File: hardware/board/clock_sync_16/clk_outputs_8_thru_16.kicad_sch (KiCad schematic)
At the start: 40 parts, among them J2 AudioJack3, U5 ISO6521FREUR

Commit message: route pcb v0.1
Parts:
- removed C10 (x16): 1uF, Capacitor_SMD:C_0402_1005Metric, symbol Device:C
- removed D1 (x8): D_TVS, Diode_SMD:D_0402_1005Metric, symbol Device:D_TVS
- removed J2 (x8): AudioJack3, Connector_Audio:Jack_3.5mm_CUI_SJ-3523-SMT_Horizontal, symbol Connector:AudioJack3
- removed U5 (x8): ISO6521FREUR, kicad_component_library:DFN-8_3x2mm_P0.5mm, symbol kicad_component_library:ISO6521FREUR
- added C10 (x16): 1uF, Capacitor_SMD:C_0402_1005Metric, symbol Device:C
- added D1 (x8): D_TVS, Diode_SMD:D_0402_1005Metric, symbol Device:D_TVS
- added D11, D12, D22, D26, D27, D28, D29, D8: LED, LED_SMD:LED_0603_1608Metric_Pad1.05x0.95mm_HandSolder, symbol Device:LED
- added J2 (x8): AudioJack3, kicad_component_library:Jack_3.5mm_Kycon_STX-3680-5NB_Vertical, symbol Connector:AudioJack3
- added R13, R14, R15, R16, R4, R5, R6, R7: R, Resistor_SMD:R_0402_1005Metric, symbol Device:R
- added U5 (x8): ISO6521FREUR, kicad_component_library:DFN-8_3x2mm_P0.5mm, symbol kicad_component_library:ISO6521FREUR
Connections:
- net +3.3V: now also C10.1, C10.1, C10.1, C10.1, C10.1, C10.1, C10.1, C10.1, U5.1 (VCC1), U5.1 (VCC1), U5.1 (VCC1), U5.1 (VCC1), U5.1 (VCC1), U5.1 (VCC1), U5.1 (VCC1), U5.1 (VCC1)
- net CH10_CONNECTED: now also U5.2 (OUT)
- net CH11_CONNECTED: now also U5.2 (OUT)
- net CH12_CONNECTED: now also U5.2 (OUT)
- net CH13_CONNECTED: now also U5.2 (OUT)
- net CH14_CONNECTED: now also U5.2 (OUT)
- net CH15_CONNECTED: now also U5.2 (OUT)
- net CH8_CONNECTED: now also U5.2 (OUT)
- net CH9_CONNECTED: now also U5.2 (OUT)
- net GND: now also C10.2, C10.2, C10.2, C10.2, C10.2, C10.2, C10.2, C10.2, U5.4 (GND1), U5.4 (GND1), U5.4 (GND1), U5.4 (GND1), U5.4 (GND1), U5.4 (GND1), U5.4 (GND1), U5.4 (GND1)
- net HARP_CLKOUT: now also U5.3 (INB), U5.3 (INB), U5.3 (INB), U5.3 (INB), U5.3 (INB), U5.3 (INB), U5.3 (INB), U5.3 (INB)
- new net: C10.2, D1.1 (A1), D28.1 (K), J2.S, U5.5 (GND2)
- new net: D1.2 (A2), J2.T, U5.6 (OUTB) (x8)
- new net: C10.1, J2.R, R15.1, U5.7 (INA), U5.8 (VCC2)
- new net: C10.2, D1.1 (A1), D29.1 (K), J2.S, U5.5 (GND2)
- new net: C10.2, D1.1 (A1), D26.1 (K), J2.S, U5.5 (GND2)
- new net: C10.1, J2.R, R4.1, U5.7 (INA), U5.8 (VCC2)
- new net: C10.2, D1.1 (A1), D22.1 (K), J2.S, U5.5 (GND2)
- new net: C10.2, D1.1 (A1), D11.1 (K), J2.S, U5.5 (GND2)
- new net: C10.2, D1.1 (A1), D8.1 (K), J2.S, U5.5 (GND2)
- new net: C10.1, J2.R, R14.1, U5.7 (INA), U5.8 (VCC2)
- new net: C10.2, D1.1 (A1), D27.1 (K), J2.S, U5.5 (GND2)
- new net: D27.2 (A), R14.2
- new net: C10.1, J2.R, R13.1, U5.7 (INA), U5.8 (VCC2)
- new net: D28.2 (A), R15.2
- new net: C10.1, J2.R, R6.1, U5.7 (INA), U5.8 (VCC2)
- new net: D11.2 (A), R6.2
- new net: D8.2 (A), R5.2
- new net: C10.1, J2.R, R5.1, U5.7 (INA), U5.8 (VCC2)
- new net: D29.2 (A), R16.2
- new net: C10.1, J2.R, R16.1, U5.7 (INA), U5.8 (VCC2)
- new net: C10.2, D1.1 (A1), D12.1 (K), J2.S, U5.5 (GND2)
- new net: D12.2 (A), R7.2
- new net: C10.1, J2.R, R7.1, U5.7 (INA), U5.8 (VCC2)
- new net: D26.2 (A), R13.2
- new net: D22.2 (A), R4.2
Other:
- note removed: "Harp Clk Sync ESD Protection. Near J1."
- note removed: "Harp Clock Sync Emitter (UART0)"

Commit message: draft firmware
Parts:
- removed C10 (x16): 1uF, Capacitor_SMD:C_0402_1005Metric, symbol Device:C
- added C2 (x16): 100nF, Capacitor_SMD:C_0402_1005Metric, symbol Device:C
- R13, R14, R15, R16, R4, R5, R6, R7: value R -> 330; Link (none) -> https://www.digikey.com/en/products/detail/yageo/RC0402FR-0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
- U5: Manufacturer (none) -> Texas Instruments; Manufacturer Number (none) -> ISO6521FREUR
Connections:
- net +3.3V: now also C2.2, C2.2, C2.2, C2.2, C2.2, C2.2, C2.2, C2.2
- net GND: now also C2.1, C2.1, C2.1, C2.1, C2.1, C2.1, C2.1, C2.1
- net at D1.1 (A1), D28.1 (K), J2.S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: now also C2.2
- net at J2.R, R15.1, U5.7 (INA)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: now also C2.1
- net at D1.1 (A1), D29.1 (K), J2.S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: now also C2.2
- net at D1.1 (A1), D26.1 (K), J2.S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: now also C2.2
- net at J2.R, R4.1, U5.7 (INA)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: now also C2.1
- net at D1.1 (A1), D22.1 (K), J2.S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: now also C2.2
- net at D1.1 (A1), D11.1 (K), J2.S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: now also C2.2
- net at D1.1 (A1), D8.1 (K), J2.S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: now also C2.2
- net at J2.R, R14.1, U5.7 (INA)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: now also C2.1
- net at D1.1 (A1), D27.1 (K), J2.S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: now also C2.2
- net at J2.R, R13.1, U5.7 (INA)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: now also C2.1
- net at J2.R, R6.1, U5.7 (INA)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: now also C2.1
- net at J2.R, R5.1, U5.7 (INA)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: now also C2.1
- net at J2.R, R16.1, U5.7 (INA)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: now also C2.1
- net at D1.1 (A1), D12.1 (K), J2.S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: now also C2.2
- net at J2.R, R7.1, U5.7 (INA)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: now also C2.1

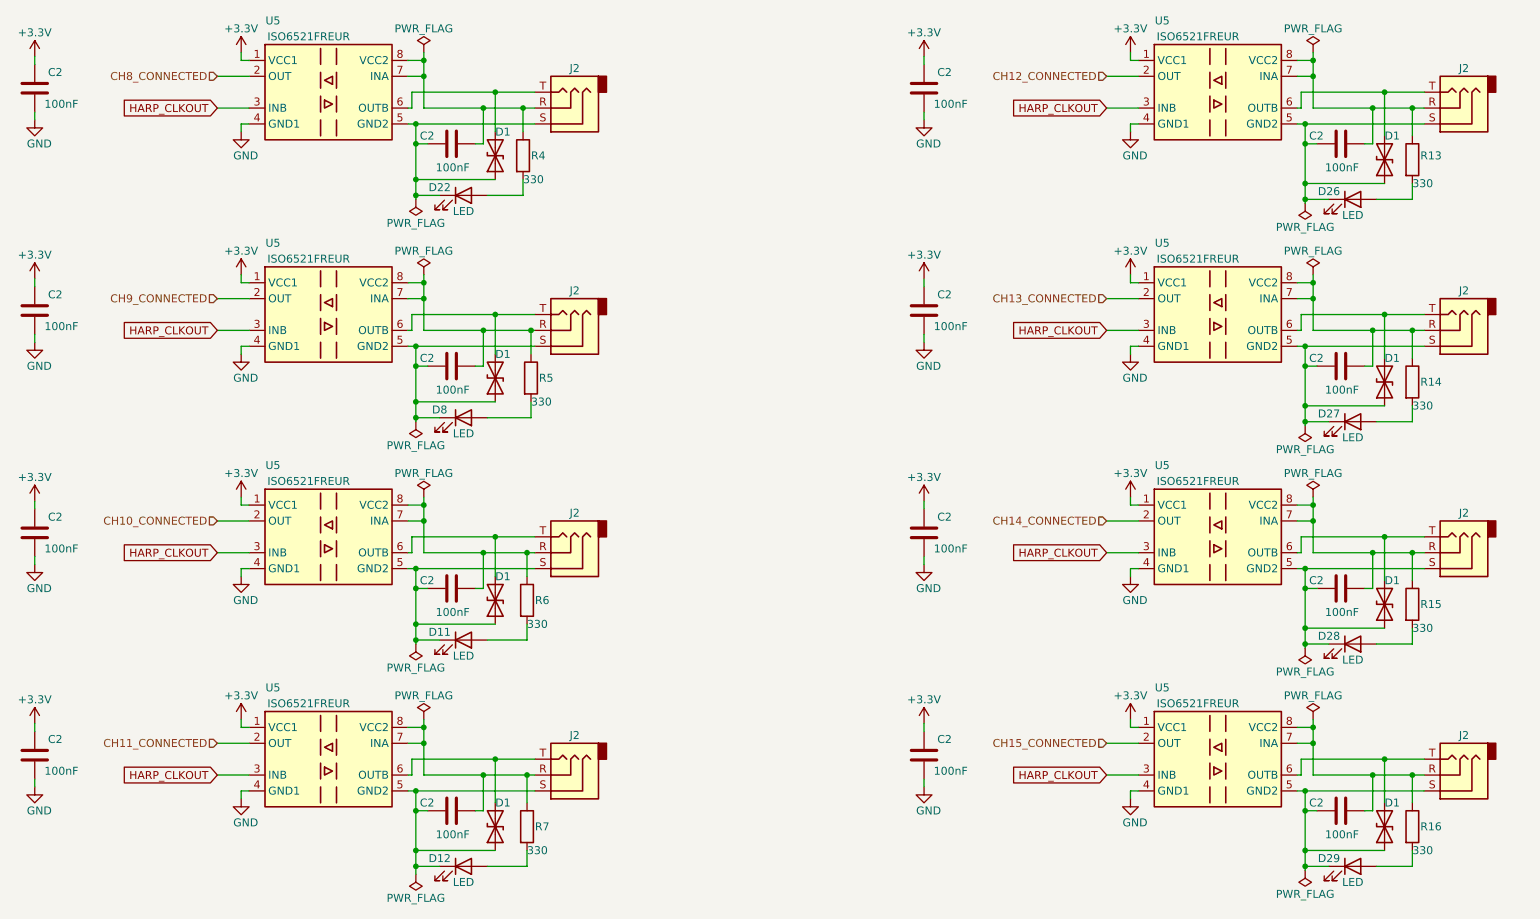
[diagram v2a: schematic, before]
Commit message: add pps/slow_uart output options
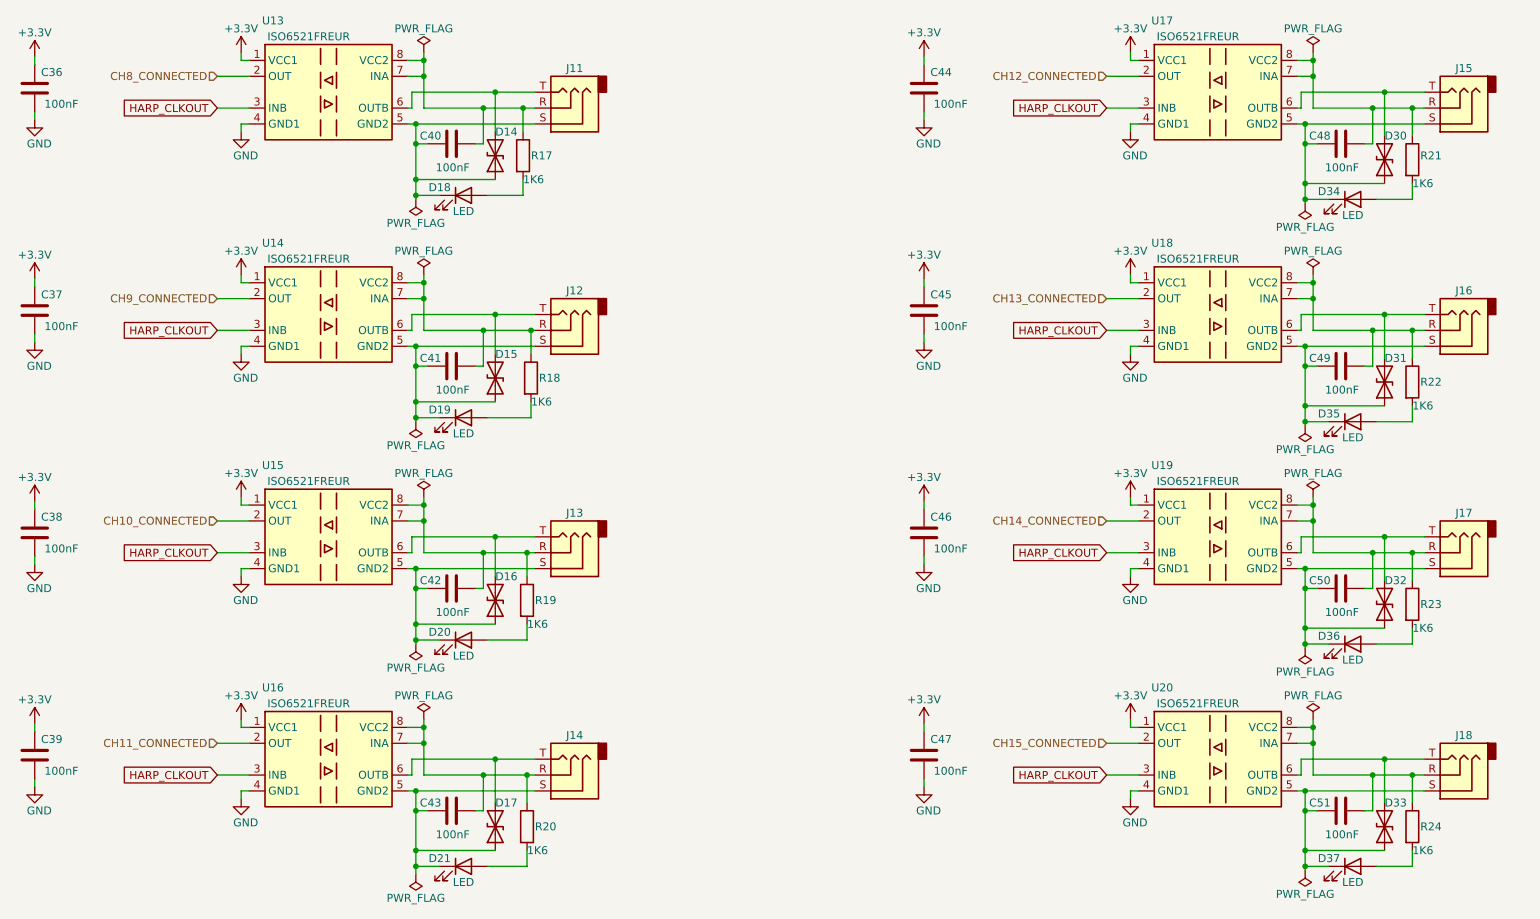
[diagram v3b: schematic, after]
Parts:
- R17: renamed from R4; value 330 -> 1K6; Link https://www.digikey.com/en/products/detail/yageo/RC0402FR-0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 -> https://www.digikey.com/en/products/detail/panasonic-electr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; Manufacturer Number RC0402FR-07330RL -> ERJ-2RKF1601X
- R18: renamed from R5; value 330 -> 1K6; Link https://www.digikey.com/en/products/detail/yageo/RC0402FR-0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 -> https://www.digikey.com/en/products/detail/panasonic-electr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; Manufacturer Number RC0402FR-07330RL -> ERJ-2RKF1601X
- R19: renamed from R6; value 330 -> 1K6; Link https://www.digikey.com/en/products/detail/yageo/RC0402FR-0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 -> https://www.digikey.com/en/products/detail/panasonic-electr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; Manufacturer Number RC0402FR-07330RL -> ERJ-2RKF1601X
- R20: renamed from R7; value 330 -> 1K6; Link https://www.digikey.com/en/products/detail/yageo/RC0402FR-0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 -> https://www.digikey.com/en/products/detail/panasonic-electr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; Manufacturer Number RC0402FR-07330RL -> ERJ-2RKF1601X
- R21: renamed from R13; value 330 -> 1K6; Link https://www.digikey.com/en/products/detail/yageo/RC0402FR-0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 -> https://www.digikey.com/en/products/detail/panasonic-electr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; Manufacturer Number RC0402FR-07330RL -> ERJ-2RKF1601X
- R22: renamed from R14; value 330 -> 1K6; Link https://www.digikey.com/en/products/detail/yageo/RC0402FR-0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 -> https://www.digikey.com/en/products/detail/panasonic-electr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; Manufacturer Number RC0402FR-07330RL -> ERJ-2RKF1601X
- R23: renamed from R15; value 330 -> 1K6; Link https://www.digikey.com/en/products/detail/yageo/RC0402FR-0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 -> https://www.digikey.com/en/products/detail/panasonic-electr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; Manufacturer Number RC0402FR-07330RL -> ERJ-2RKF1601X
- R24: renamed from R16; value 330 -> 1K6; Link https://www.digikey.com/en/products/detail/yageo/RC0402FR-0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 -> https://www.digikey.com/en/products/detail/panasonic-electr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; Manufacturer Number RC0402FR-07330RL -> ERJ-2RKF1601X
- renumbered C2 to C36, C2 to C37, C2 to C38, C2 to C39, C2 to C40, C2 to C41, C2 to C42, C2 to C43, C2 to C44, C2 to C45, C2 to C46, C2 to C47, C2 to C48, C2 to C49, C2 to C50, C2 to C51, D1 to D14, D1 to D15, D1 to D16, D1 to D17, D22 to D18, D8 to D19, D11 to D20, D12 to D21, D1 to D30, D1 to D31, D1 to D32, D1 to D33, D26 to D34, D27 to D35, D28 to D36, D29 to D37, J2 to J11, J2 to J12, J2 to J13, J2 to J14, J2 to J15, J2 to J16, J2 to J17, J2 to J18, U5 to U13, U5 to U14, U5 to U15, U5 to U16, U5 to U17, U5 to U18, U5 to U19, U5 to U20

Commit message: update harp core; update led resistors and deprecated parts; bump versions
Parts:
- D14, D15, D16, D17, D30, D31, D32, D33: Link https://www.digikey.com/en/products/detail/onsemi/ESD7571N2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 -> https://www.digikey.com/en/products/detail/nexperia-usa-inc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; Manufacturer Number ESD7571N2T5G -> PESD5V0F1BLD,315
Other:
- company: (none) -> The Allen Institute
- title: (none) -> harp.device.white-rabbit
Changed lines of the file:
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@@
 	(generator_version "8.0")
 	(paper "A4")
+	(title_block
+		(title "harp.device.white-rabbit")
+		(date "2025-02-21")
+		(rev "1.0.0")
+		(company "The Allen Institute")
+	)
 	(junction
 		(at 91.44 26.035)
@@
 			)
 		)
-		(property "Datasheet" "https://www.onsemi.com/pdf/datasheet/esd7571-d.pdf"
+		(property "Datasheet" "https://assets.nexperia.com/documents/data-sheet/PESD5V0F1BLD.pdf"
 			(at 245.11 146.05 0)
 			(effects
@@
 			)
 		)
-		(property "Link" "https://www.digikey.com/en/products/detail/onsemi/ESD7571N2T5G/7220690"
+		(property "Link" "https://www.digikey.com/en/products/detail/nexperia-usa-inc/PESD5V0F1BLD-315/3679473"
 			(at 245.11 146.05 0)
 			(effects
@@
 			)
 		)
-		(property "Manufacturer Number" "ESD7571N2T5G"
+		(property "Manufacturer Number" "PESD5V0F1BLD,315"
 			(at 245.11 146.05 0)
 			(effects
@@
 			)
 		)
-		(property "Datasheet" "https://www.onsemi.com/pdf/datasheet/esd7571-d.pdf"
+		(property "Datasheet" "https://assets.nexperia.com/documents/data-sheet/PESD5V0F1BLD.pdf"
 			(at 245.11 39.37 0)
 			(effects
@@
 			)
 		)
-		(property "Link" "https://www.digikey.com/en/products/detail/onsemi/ESD7571N2T5G/7220690"
+		(property "Link" "https://www.digikey.com/en/products/detail/nexperia-usa-inc/PESD5V0F1BLD-315/3679473"
 			(at 245.11 39.37 0)
 			(effects
@@
 			)
 		)
-		(property "Manufacturer Number" "ESD7571N2T5G"
+		(property "Manufacturer Number" "PESD5V0F1BLD,315"
 			(at 245.11 39.37 0)
 			(effects
@@
 			)
 		)
-		(property "Datasheet" "https://www.onsemi.com/pdf/datasheet/esd7571-d.pdf"
+		(property "Datasheet" "https://assets.nexperia.com/documents/data-sheet/PESD5V0F1BLD.pdf"
 			(at 102.87 109.855 0)
 			(effects
@@
 			)
 		)
-		(property "Link" "https://www.digikey.com/en/products/detail/onsemi/ESD7571N2T5G/7220690"
+		(property "Link" "https://www.digikey.com/en/products/detail/nexperia-usa-inc/PESD5V0F1BLD-315/3679473"
 			(at 102.87 109.855 0)
 			(effects
@@
 			)
 		)
-		(property "Manufacturer Number" "ESD7571N2T5G"
+		(property "Manufacturer Number" "PESD5V0F1BLD,315"
 			(at 102.87 109.855 0)
 			(effects
@@
 			)
 		)
-		(property "Datasheet" "https://www.onsemi.com/pdf/datasheet/esd7571-d.pdf"
+		(property "Datasheet" "https://assets.nexperia.com/documents/data-sheet/PESD5V0F1BLD.pdf"
 			(at 102.87 74.295 0)
 			(effects
@@
 			)
 		)
-		(property "Link" "https://www.digikey.com/en/products/detail/onsemi/ESD7571N2T5G/7220690"
+		(property "Link" "https://www.digikey.com/en/products/detail/nexperia-usa-inc/PESD5V0F1BLD-315/3679473"
 			(at 102.87 74.295 0)
 			(effects
@@
 			)
 		)
-		(property "Manufacturer Number" "ESD7571N2T5G"
+		(property "Manufacturer Number" "PESD5V0F1BLD,315"
 			(at 102.87 74.295 0)
 			(effects
@@
 			)
 		)
-		(property "Datasheet" "https://www.onsemi.com/pdf/datasheet/esd7571-d.pdf"
+		(property "Datasheet" "https://assets.nexperia.com/documents/data-sheet/PESD5V0F1BLD.pdf"
 			(at 245.11 74.93 0)
 			(effects
@@
 			)
 		)
-		(property "Link" "https://www.digikey.com/en/products/detail/onsemi/ESD7571N2T5G/7220690"
+		(property "Link" "https://www.digikey.com/en/products/detail/nexperia-usa-inc/PESD5V0F1BLD-315/3679473"
 			(at 245.11 74.93 0)
 			(effects
@@
 			)
 		)
-		(property "Manufacturer Number" "ESD7571N2T5G"
+		(property "Manufacturer Number" "PESD5V0F1BLD,315"
 			(at 245.11 74.93 0)
 			(effects
@@
 			)
 		)
-		(property "Datasheet" "https://www.onsemi.com/pdf/datasheet/esd7571-d.pdf"
+		(property "Datasheet" "https://assets.nexperia.com/documents/data-sheet/PESD5V0F1BLD.pdf"
 			(at 245.11 110.49 0)
 			(effects
@@
 			)
 		)
-		(property "Link" "https://www.digikey.com/en/products/detail/onsemi/ESD7571N2T5G/7220690"
+		(property "Link" "https://www.digikey.com/en/products/detail/nexperia-usa-inc/PESD5V0F1BLD-315/3679473"
 			(at 245.11 110.49 0)
 			(effects
@@
 			)
 		)
-		(property "Manufacturer Number" "ESD7571N2T5G"
+		(property "Manufacturer Number" "PESD5V0F1BLD,315"
 			(at 245.11 110.49 0)
 			(effects
@@
 			)
 		)
-		(property "Datasheet" "https://www.onsemi.com/pdf/datasheet/esd7571-d.pdf"
+		(property "Datasheet" "https://assets.nexperia.com/documents/data-sheet/PESD5V0F1BLD.pdf"
 			(at 102.87 146.05 0)
 			(effects
@@
 			)
 		)
-		(property "Link" "https://www.digikey.com/en/products/detail/onsemi/ESD7571N2T5G/7220690"
+		(property "Link" "https://www.digikey.com/en/products/detail/nexperia-usa-inc/PESD5V0F1BLD-315/3679473"
 			(at 102.87 146.05 0)
 			(effects
@@
 			)
 		)
-		(property "Manufacturer Number" "ESD7571N2T5G"
+		(property "Manufacturer Number" "PESD5V0F1BLD,315"
 			(at 102.87 146.05 0)
 			(effects
@@
 			)
 		)
-		(property "Datasheet" "https://www.onsemi.com/pdf/datasheet/esd7571-d.pdf"
+		(property "Datasheet" "https://assets.nexperia.com/documents/data-sheet/PESD5V0F1BLD.pdf"
 			(at 102.87 38.735 0)
 			(effects
@@
 			)
 		)
-		(property "Link" "https://www.digikey.com/en/products/detail/onsemi/ESD7571N2T5G/7220690"
+		(property "Link" "https://www.digikey.com/en/products/detail/nexperia-usa-inc/PESD5V0F1BLD-315/3679473"
 			(at 102.87 38.735 0)
 			(effects
@@
 			)
 		)
-		(property "Manufacturer Number" "ESD7571N2T5G"
+		(property "Manufacturer Number" "PESD5V0F1BLD,315"
 			(at 102.87 38.735 0)
 			(effects

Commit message: update missing BOM field
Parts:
- D14, D15, D16, D17, D30, D31, D32, D33: Manufacturer onsemi -> Nexperia USA Inc.
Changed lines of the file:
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@@
 			)
 		)
-		(property "Manufacturer" "onsemi"
+		(property "Manufacturer" "Nexperia USA Inc."
 			(at 245.11 146.05 0)
 			(effects
@@
 			)
 		)
-		(property "Manufacturer" "onsemi"
+		(property "Manufacturer" "Nexperia USA Inc."
 			(at 245.11 39.37 0)
 			(effects
@@
 			)
 		)
-		(property "Manufacturer" "onsemi"
+		(property "Manufacturer" "Nexperia USA Inc."
 			(at 102.87 109.855 0)
 			(effects
@@
 			)
 		)
-		(property "Manufacturer" "onsemi"
+		(property "Manufacturer" "Nexperia USA Inc."
 			(at 102.87 74.295 0)
 			(effects
@@
 			)
 		)
-		(property "Manufacturer" "onsemi"
+		(property "Manufacturer" "Nexperia USA Inc."
 			(at 245.11 74.93 0)
 			(effects
@@
 			)
 		)
-		(property "Manufacturer" "onsemi"
+		(property "Manufacturer" "Nexperia USA Inc."
 			(at 245.11 110.49 0)
 			(effects
@@
 			)
 		)
-		(property "Manufacturer" "onsemi"
+		(property "Manufacturer" "Nexperia USA Inc."
 			(at 102.87 146.05 0)
 			(effects
@@
 			)
 		)
-		(property "Manufacturer" "onsemi"
+		(property "Manufacturer" "Nexperia USA Inc."
 			(at 102.87 38.735 0)
 			(effects
